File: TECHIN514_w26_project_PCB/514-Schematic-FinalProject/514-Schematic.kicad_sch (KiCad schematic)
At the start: 15 parts, among them J1 Conn_01x02, U1 28BYJ-48, U2 MPU-6050, U3 ULN2003, U4 ESP32C3, U5 ESP32C3, U6 SSD1306

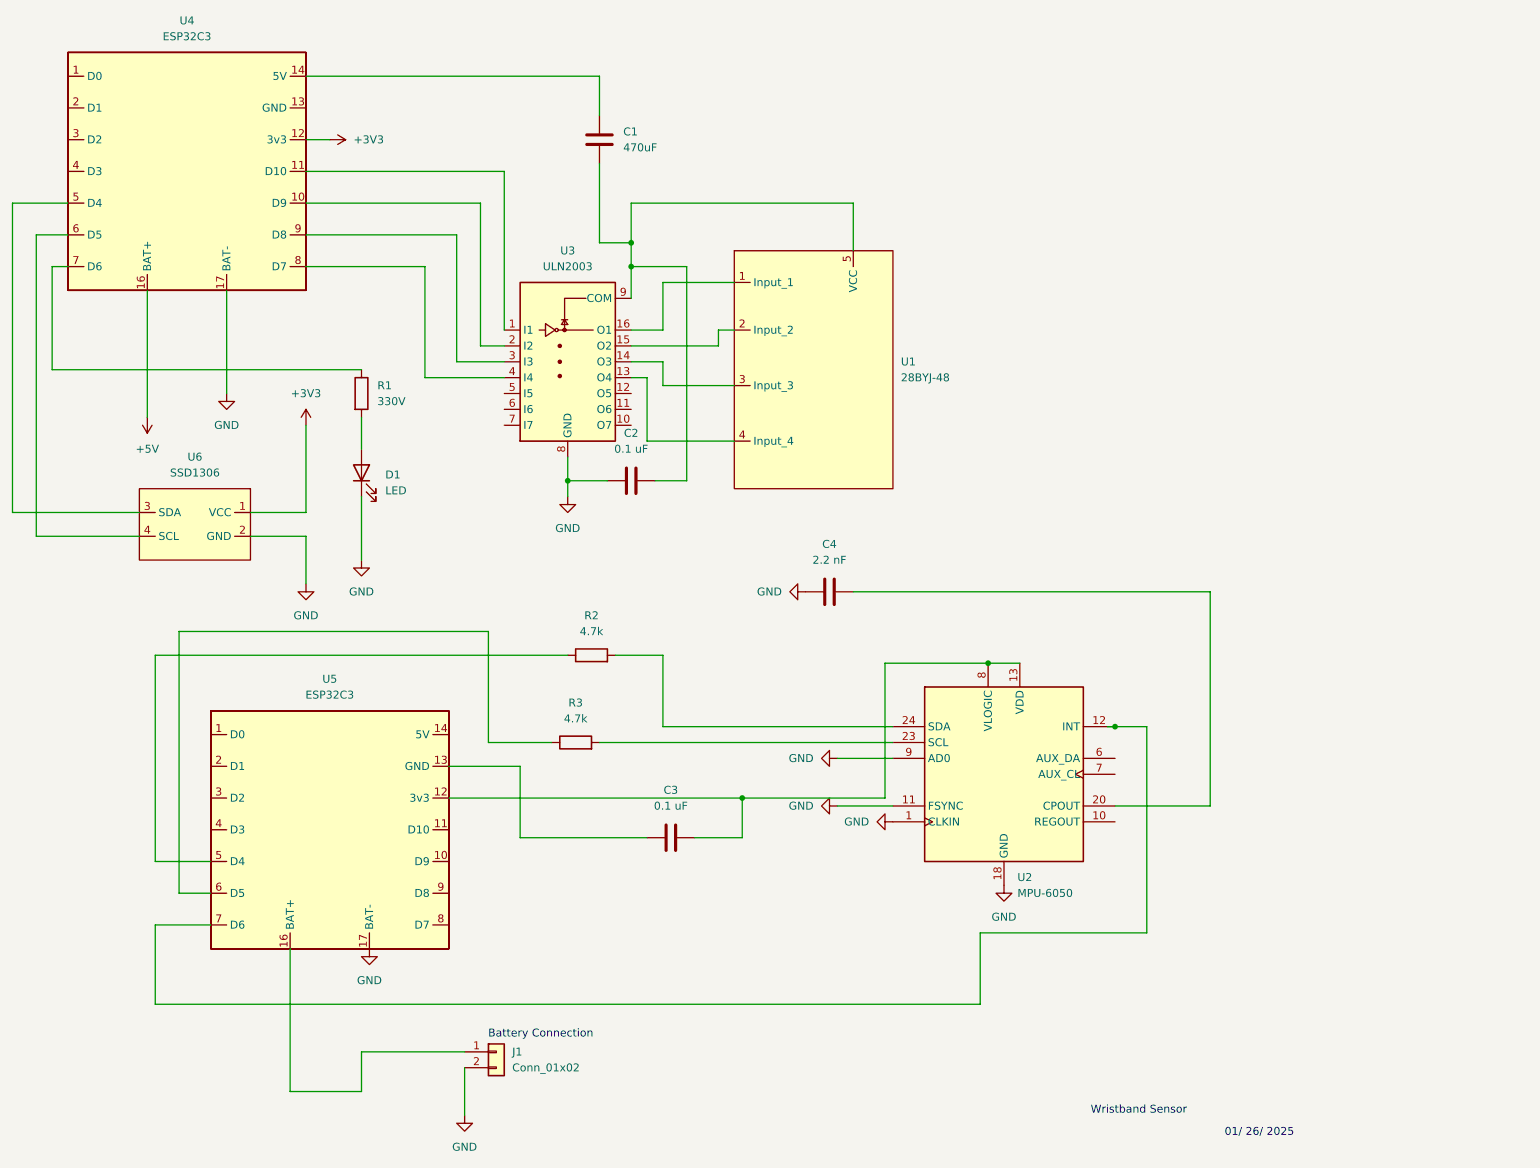
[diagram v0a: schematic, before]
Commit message: Add PCB and Code for Devices
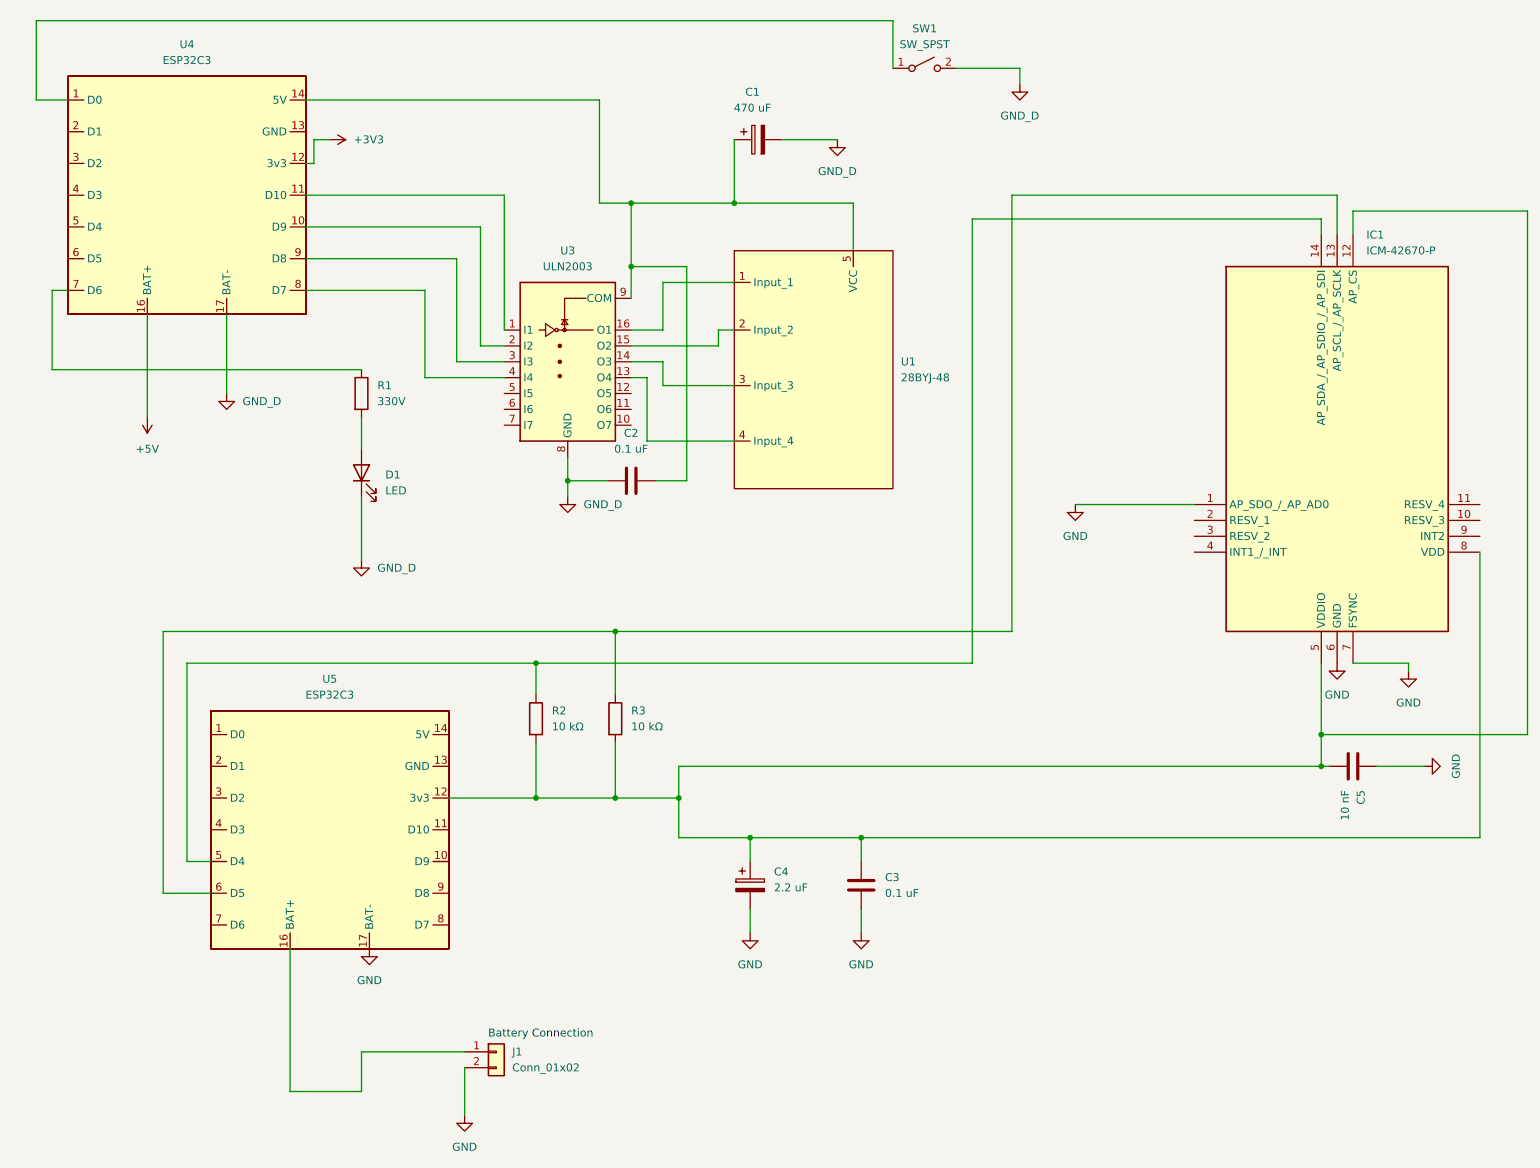
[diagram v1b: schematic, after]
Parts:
- removed C1: 470uF, Capacitor_SMD:C_0603_1608Metric_Pad1.08x0.95mm_HandSolder, symbol Device:C
- removed C4: 2.2 nF, Capacitor_SMD:C_0603_1608Metric_Pad1.08x0.95mm_HandSolder, symbol Device:C
- removed U2: MPU-6050, Sensor_Motion:InvenSense_QFN-24_4x4mm_P0.5mm, symbol Sensor_Motion:MPU-6050
- removed U6: SSD1306, Footprints:128x64OLED, symbol Personal:SSD1306
- added C1: 470 uF, Capacitor_SMD:C_0603_1608Metric_Pad1.08x0.95mm_HandSolder, symbol Device:C_Polarized
- added C4: 2.2 uF, Capacitor_SMD:C_0603_1608Metric_Pad1.08x0.95mm_HandSolder, symbol Device:C_Polarized
- added C5: 10 nF, Capacitor_SMD:C_0603_1608Metric_Pad1.08x0.95mm_HandSolder, symbol Device:C
- added IC1: ICM-42670-P, IMU:ICM42670P, symbol ICM-42670-P:ICM-42670-P
- added SW1: SW_SPST, Button_Switch_THT:SW_PUSH_6mm, symbol Switch:SW_SPST
- R2, R3: value 4.7k -> 10 kΩ
- U1: footprint Connector_JST:JST_XH_B5B-XH-A_1x05_P2.50mm_Vertical -> Connector_JST:JST_XH_B5B-XH-AM_1x05_P2.50mm_Vertical
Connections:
- net GND: now also C3.2, C4.2, C5.1, IC1.1 (AP_SDO_/_AP_AD0), IC1.6 (GND), IC1.7 (FSYNC); no longer C2.1, D1.1 (K), U3.8 (GND), U4.17 (BAT-)
- net at C3.1: now also R2.2, R3.2, U5.12 (3v3), C4.1, C5.2, IC1.12 (AP_CS), IC1.5 (VDDIO), IC1.8 (VDD); no longer U5.13 (GND)
- net at R2.1, U5.5 (D4): now also IC1.14 (AP_SDA_/_AP_SDIO_/_AP_SDI)
- net at R3.1, U5.6 (D5): now also IC1.13 (AP_SCL_/_AP_SCLK)
- net at U4.1 (D0): now also SW1.1 (A)
- net at U4.14 (5V): now also C2.2, U1.5 (VCC), U3.9 (COM), C1.1
- new net GND_D: C1.2, C2.1, D1.1 (K), SW1.2 (B), U3.8 (GND), U4.17 (BAT-)
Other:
- note removed: "01/ 26/ 2025"
- note removed: "Wristband Sensor"
- title: (none) -> Wirstband Sensor
- moved on the sheet: U4
